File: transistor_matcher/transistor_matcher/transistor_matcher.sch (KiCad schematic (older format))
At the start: 17 parts, among them J3 14x4 Segment Display (I2C), Q1 2N3904, Q2 2N3904, SW1 SW_DPDT_x2, SW2 SW_DPDT_x2, U1 AD8223, U2 LM317_3PinPackage, U3 Teensy2.0_(Arduino)

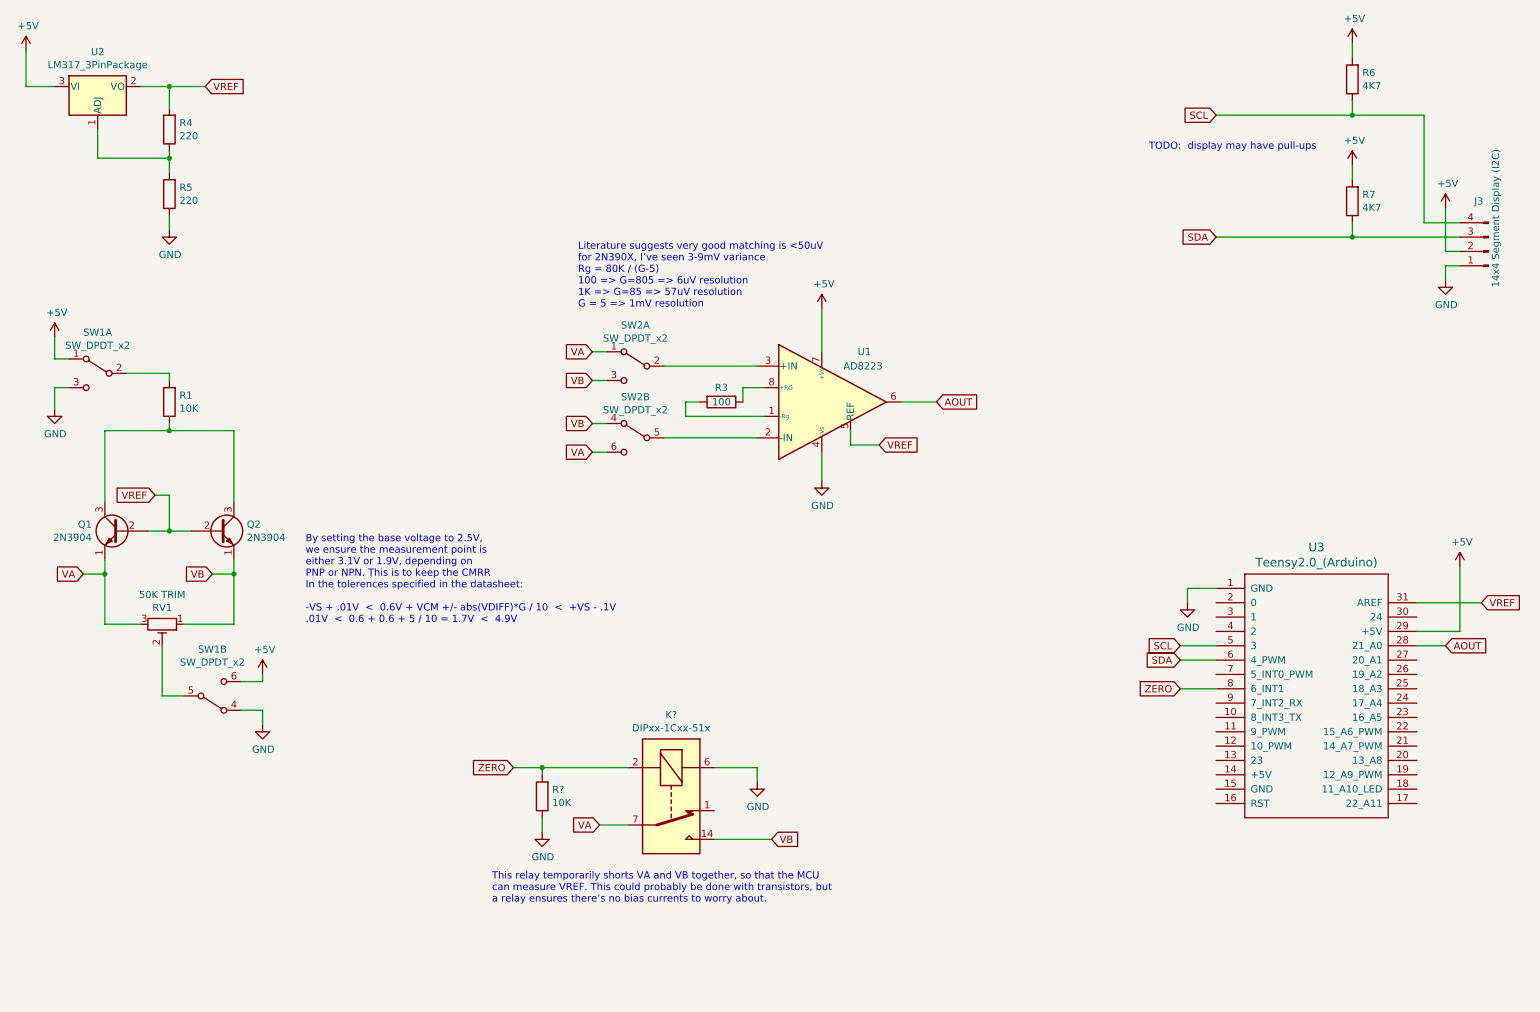
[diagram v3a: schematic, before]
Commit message: updated to include display
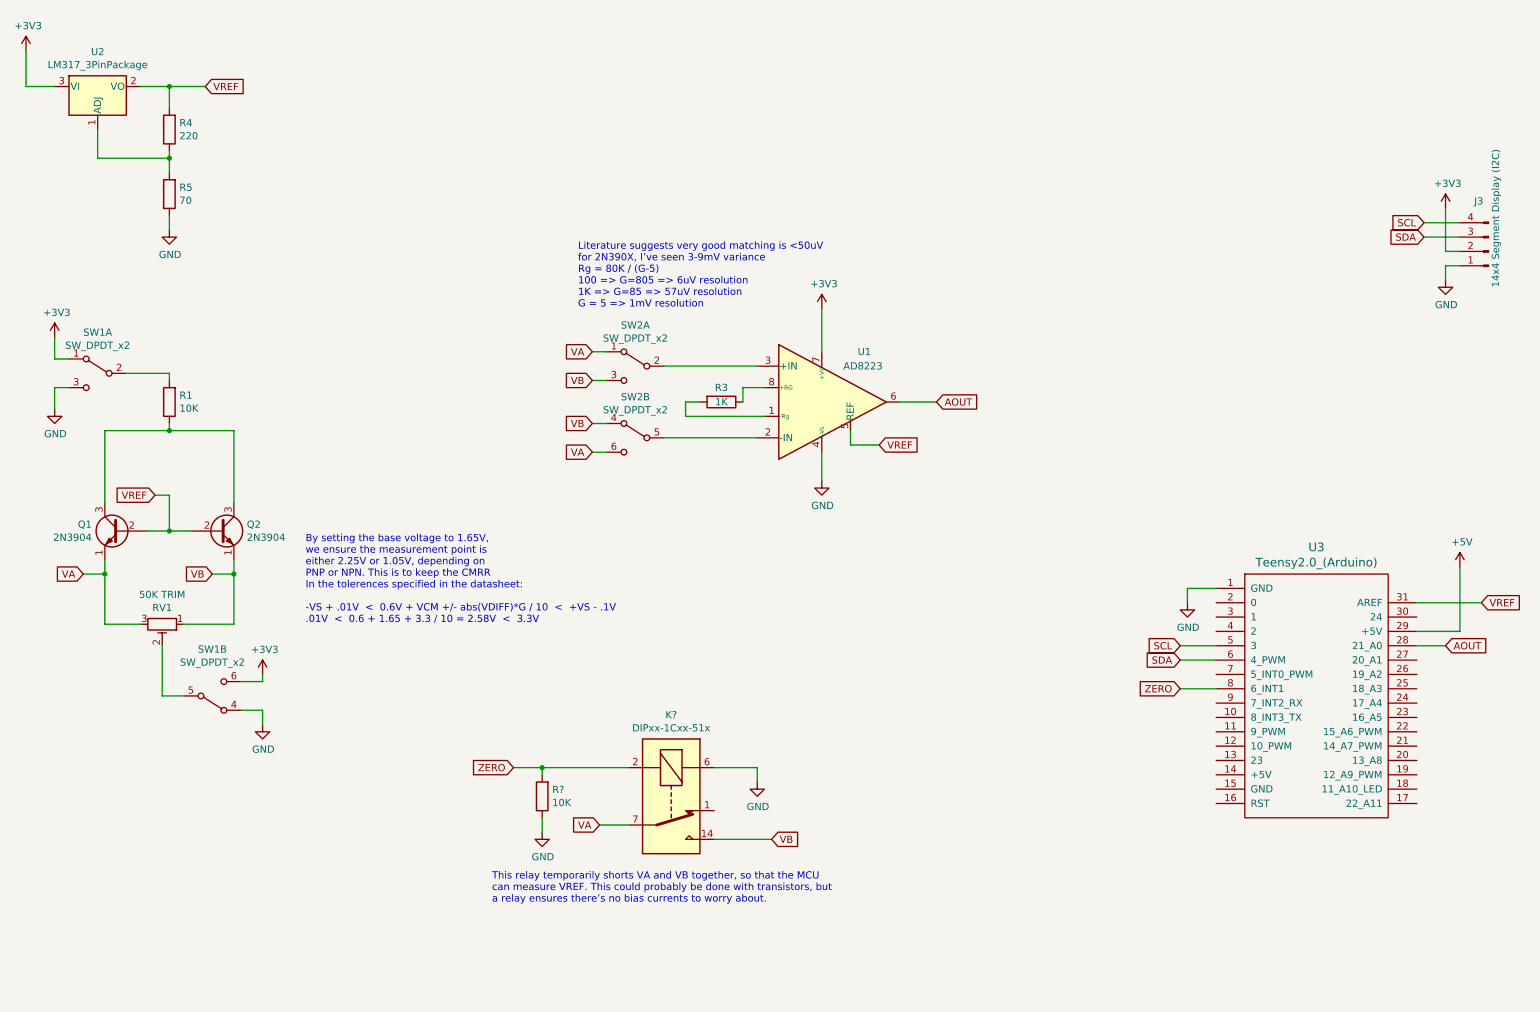
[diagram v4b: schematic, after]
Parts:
- removed R6, R7: 4K7, KiCad/Resistors_ThroughHole.pretty:R_Axial_DIN0204_L3.6mm_D1.6mm_P1.90mm_Vertical, symbol Device:R
- R3: value 100 -> 1K
- R5: value 220 -> 70
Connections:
- net +5V: no longer J3.2 (Pin_2), SW1.1 (A), SW1.6 (C), U1.7 (+Vs), U2.3 (VI)
- new net +3V3: J3.2 (Pin_2), SW1.1 (A), SW1.6 (C), U1.7 (+Vs), U2.3 (VI)
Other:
- note added: "By setting the base voltage to 1.65V,\nwe ensure the measurement point is\neither 2.25V or 1.05V, depending on\nPNP or NPN. This is to keep the CMRR\nIn the tolerences specified in the datasheet:\n\n-VS + .01V < 0.6V + VCM +/- abs(VDIFF)*G / 10 < +VS - .1V\n.01V < 0.6 + 1.65 + 3.3 / 10 = 2.58V < 3.3V"
- note removed: "By setting the base voltage to 2.5V,\nwe ensure the measurement point is\neither 3.1V or 1.9V, depending on\nPNP or NPN. This is to keep the CMRR\nIn the tolerences specified in the datasheet:\n\n-VS + .01V < 0.6V + VCM +/- abs(VDIFF)*G / 10 < +VS - .1V\n.01V < 0.6 + 0.6 + 5 / 10 = 1.7V < 4.9V"
- note removed: "TODO: display may have pull-ups"
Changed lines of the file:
@@
-	1    0    0    -1
-$EndComp
-$Comp
-L power:+5V #PWR0102
-U 1 1 5E74784D
-P 6200 2650
-F 0 "#PWR0102" H 6200 2500 50  0001 C CNN
-F 1 "+5V" H 6215 2823 50  0000 C CNN
-F 2 "" H 6200 2650 50  0001 C CNN
-F 3 "" H 6200 2650 50  0001 C CNN
-	1    6200 2650
 	1    0    0    -1
 $EndComp
@@
 P 5500 3300
 F 0 "R3" V 5400 3300 50  0000 C CNN
-F 1 "100" V 5500 3300 50  0000 C CNN
+F 1 "1K" V 5500 3300 50  0000 C CNN
 F 2 "KiCad/Resistors_ThroughHole.pretty:R_Axial_DIN0204_L3.6mm_D1.6mm_P1.90mm_Vertical" V 5430 3300 50  0001 C CNN
 F 3 "~" H 5500 3300 50  0001 C CNN
@@
 Wire Wire Line
 	5250 3300 5350 3300
-$Comp
-L power:+5V #PWR0103
-U 1 1 5E7492AC
-P 650 850
-F 0 "#PWR0103" H 650 700 50  0001 C CNN
-F 1 "+5V" H 665 1023 50  0000 C CNN
-F 2 "" H 650 850 50  0001 C CNN
-F 3 "" H 650 850 50  0001 C CNN
-	1    650  850
-	1    0    0    -1
-$EndComp
 $Comp
 L power:GND #PWR0104
@@
 P 1650 1850
 F 0 "R5" H 1580 1804 50  0000 R CNN
-F 1 "220" H 1580 1895 50  0000 R CNN
+F 1 "70" H 1580 1895 50  0000 R CNN
 F 2 "KiCad/Resistors_ThroughHole.pretty:R_Axial_DIN0204_L3.6mm_D1.6mm_P1.90mm_Vertical" V 1580 1850 50  0001 C CNN
 F 3 "~" H 1650 1850 50  0001 C CNN
@@
 $EndComp
 Text Notes 2600 4850 0    50   ~ 0
-By setting the base voltage to 2.5V,\nwe ensure the measurement point is\neither 3.1V or 1.9V, depending on\nPNP or NPN. This is to keep the CMRR\nIn the tolerences specified in the datasheet:\n\n-VS + .01V  <  0.6V + VCM +/- abs(VDIFF)*G / 10  <  +VS - .1V\n.01V  <  0.6 + 0.6 + 5 / 10 = 1.7V  <  4.9V
+By setting the base voltage to 1.65V,\nwe ensure the measurement point is\neither 2.25V or 1.05V, depending on\nPNP or NPN. This is to keep the CMRR\nIn the tolerences specified in the datasheet:\n\n-VS + .01V  <  0.6V + VCM +/- abs(VDIFF)*G / 10  <  +VS - .1V\n.01V  <  0.6 + 1.65 + 3.3 / 10 = 2.58V  <  3.3V
 Text GLabel 1900 1100 2    50   Input ~ 0
 VREF
@@
 VB
 $Comp
-L power:+5V #PWR0105
-U 1 1 5E7609E6
-P 850 2850
-F 0 "#PWR0105" H 850 2700 50  0001 C CNN
-F 1 "+5V" H 865 3023 50  0000 C CNN
-F 2 "" H 850 2850 50  0001 C CNN
-F 3 "" H 850 2850 50  0001 C CNN
-	1    850  2850
-	1    0    0    -1
-$EndComp
-$Comp
 L power:GND #PWR0106
 U 1 1 5E7616F7
@@
 Text GLabel 8700 5000 0    50   Input ~ 0
 SCL
-$Comp
-L Device:R R6
-U 1 1 5E7A0721
-P 9900 1050
-F 0 "R6" H 9830 1004 50  0000 R CNN
-F 1 "4K7" H 9830 1095 50  0000 R CNN
-F 2 "KiCad/Resistors_ThroughHole.pretty:R_Axial_DIN0204_L3.6mm_D1.6mm_P1.90mm_Vertical" V 9830 1050 50  0001 C CNN
-F 3 "~" H 9900 1050 50  0001 C CNN
-	1    9900 1050
-	-1   0    0    1
-$EndComp
-Wire Wire Line
-	9900 1200 9900 1300
-$Comp
-L power:+5V #PWR0113
-U 1 1 5E7A8C07
-P 9900 800
-F 0 "#PWR0113" H 9900 650 50  0001 C CNN
-F 1 "+5V" H 9915 973 50  0000 C CNN
-F 2 "" H 9900 800 50  0001 C CNN
-F 3 "" H 9900 800 50  0001 C CNN
-	1    9900 800
-	1    0    0    -1
-$EndComp
-Wire Wire Line
-	9900 800  9900 900
-Connection ~ 9900 1300
-$Comp
-L Device:R R7
-U 1 1 5E7B97AD
-P 9900 1900
-F 0 "R7" H 9830 1854 50  0000 R CNN
-F 1 "4K7" H 9830 1945 50  0000 R CNN
-F 2 "KiCad/Resistors_ThroughHole.pretty:R_Axial_DIN0204_L3.6mm_D1.6mm_P1.90mm_Vertical" V 9830 1900 50  0001 C CNN
-F 3 "~" H 9900 1900 50  0001 C CNN
-	1    9900 1900
-	-1   0    0    1
-$EndComp
-Wire Wire Line
-	9900 2050 9900 2150
-$Comp
-L power:+5V #PWR0114
-U 1 1 5E7B97B8
-P 9900 1650
-F 0 "#PWR0114" H 9900 1500 50  0001 C CNN
-F 1 "+5V" H 9915 1823 50  0000 C CNN
-F 2 "" H 9900 1650 50  0001 C CNN
-F 3 "" H 9900 1650 50  0001 C CNN
-	1    9900 1650
-	1    0    0    -1
-$EndComp
-Wire Wire Line
-	9900 1650 9900 1750
-Connection ~ 9900 2150
-Text Notes 9650 1550 2    50   ~ 0
-TODO:  display may have pull-ups
 $Comp
 L Connector:Conn_01x04_Male J3
@@
 	1    0    0    -1
 $EndComp
-Text GLabel 8950 1300 0    50   Input ~ 0
+Text GLabel 10400 2050 0    50   Input ~ 0
 SCL
-Text GLabel 8950 2150 0    50   Input ~ 0
+Text GLabel 10400 2150 0    50   Input ~ 0
 SDA
 Wire Wire Line
-	9900 2150 10650 2150
-Wire Wire Line
-	10400 1300 10400 2050
-Wire Wire Line
 	10400 2050 10650 2050
-Wire Wire Line
-	9900 1300 10400 1300
-$Comp
-L power:+5V #PWR0116
-U 1 1 5E82BCFC
-P 10550 1950
-F 0 "#PWR0116" H 10550 1800 50  0001 C CNN
-F 1 "+5V" H 10565 2123 50  0000 C CNN
-F 2 "" H 10550 1950 50  0001 C CNN
-F 3 "" H 10550 1950 50  0001 C CNN
-	1    10550 1950
-	1    0    0    -1
-$EndComp
 Wire Wire Line
 	10550 1950 10550 2250
@@
 Wire Wire Line
 	2300 5450 2150 5450
-$Comp
-L power:+5V #PWR0117
-U 1 1 5E7BAA7F
-P 2300 5200
-F 0 "#PWR0117" H 2300 5050 50  0001 C CNN
-F 1 "+5V" H 2315 5373 50  0000 C CNN
-F 2 "" H 2300 5200 50  0001 C CNN
-F 3 "" H 2300 5200 50  0001 C CNN
-	1    2300 5200
-	1    0    0    -1
-$EndComp
 Wire Wire Line
 	2300 5200 2300 5250
@@
 Wire Wire Line
 	1650 4200 1800 4200
-Wire Wire Line
-	8950 2150 9900 2150
-Wire Wire Line
-	8950 1300 9900 1300
 $Comp
 L teensy:Teensy2.0_(Arduino) U3
@@
 Wire Wire Line
 	4250 6300 4250 6200
+$Comp
+L power:+3V3 #PWR?
+U 1 1 5E81E7F2
+P 650 850
+F 0 "#PWR?" H 650 700 50  0001 C CNN
+F 1 "+3V3" H 665 1023 50  0000 C CNN
+F 2 "" H 650 850 50  0001 C CNN
+F 3 "" H 650 850 50  0001 C CNN
+	1    650  850
+	1    0    0    -1
+$EndComp
+$Comp
+L power:+3V3 #PWR?
+U 1 1 5E821492
+P 850 2850
+F 0 "#PWR?" H 850 2700 50  0001 C CNN
+F 1 "+3V3" H 865 3023 50  0000 C CNN
+F 2 "" H 850 2850 50  0001 C CNN
+F 3 "" H 850 2850 50  0001 C CNN
+	1    850  2850
+	1    0    0    -1
+$EndComp
+$Comp
+L power:+3V3 #PWR?
+U 1 1 5E824339
+P 6200 2650
+F 0 "#PWR?" H 6200 2500 50  0001 C CNN
+F 1 "+3V3" H 6215 2823 50  0000 C CNN
+F 2 "" H 6200 2650 50  0001 C CNN
+F 3 "" H 6200 2650 50  0001 C CNN
+	1    6200 2650
+	1    0    0    -1
+$EndComp
+$Comp
+L power:+3V3 #PWR?
+U 1 1 5E827555
+P 10550 1950
+F 0 "#PWR?" H 10550 1800 50  0001 C CNN
+F 1 "+3V3" H 10565 2123 50  0000 C CNN
+F 2 "" H 10550 1950 50  0001 C CNN
+F 3 "" H 10550 1950 50  0001 C CNN
+	1    10550 1950
+	1    0    0    -1
+$EndComp
+$Comp
+L power:+3V3 #PWR?
+U 1 1 5E82FB83
+P 2300 5200
+F 0 "#PWR?" H 2300 5050 50  0001 C CNN
+F 1 "+3V3" H 2315 5373 50  0000 C CNN
+F 2 "" H 2300 5200 50  0001 C CNN
+F 3 "" H 2300 5200 50  0001 C CNN
+	1    2300 5200
+	1    0    0    -1
+$EndComp
+Wire Wire Line
+	10400 2150 10650 2150
 $EndSCHEMATC
